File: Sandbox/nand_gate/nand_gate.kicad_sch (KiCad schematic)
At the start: 10 parts, among them Q1 2N3904, Q2 2N3904, Q3 2N3904, SW1 SW_SPST, SW2 SW_SPST

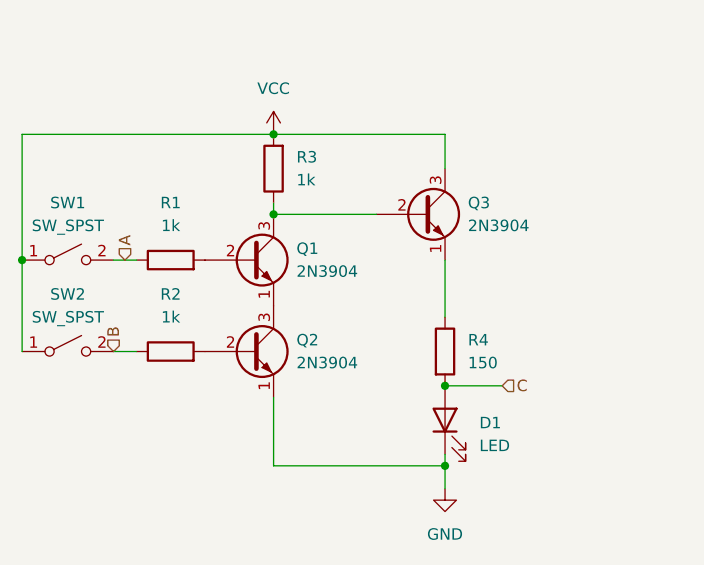
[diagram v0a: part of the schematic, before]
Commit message: Layout for nand gate
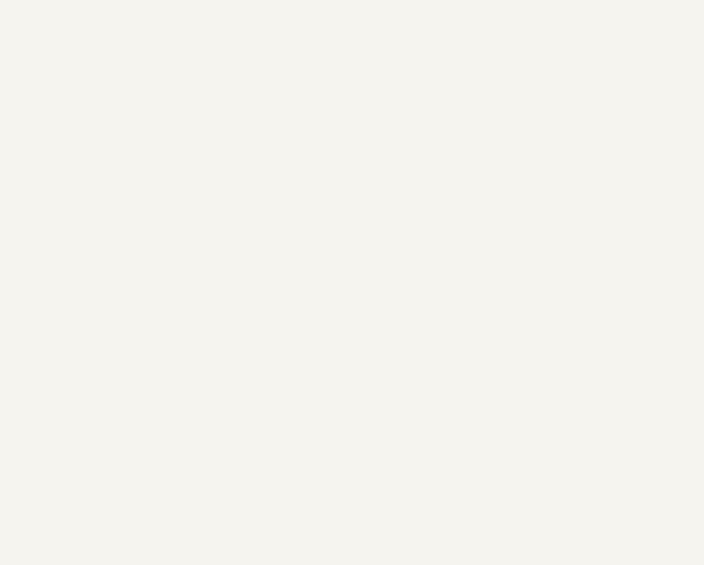
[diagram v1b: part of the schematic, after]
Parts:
- removed D1: LED, LED_THT:LED_D5.0mm, symbol Device:LED
- removed Q1, Q2, Q3: 2N3904, Package_TO_SOT_THT:TO-92_Inline, symbol Transistor_BJT:2N3904
- removed R1, R2, R3: 1k, Resistor_THT:R_Axial_DIN0207_L6.3mm_D2.5mm_P7.62mm_Horizontal, symbol Device:R
- removed R4: 150, Resistor_THT:R_Axial_DIN0207_L6.3mm_D2.5mm_P7.62mm_Horizontal, symbol Device:R
- removed SW1, SW2: SW_SPST, Button_Switch_THT:SW_PUSH_6mm, symbol Switch:SW_SPST

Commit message: Moved Some Things Around
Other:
- added sheet nand_gate7 (nand__gate.kicad_sch)
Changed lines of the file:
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@@
+    )
+  )
+  (sheet (at 83.82 114.3) (size 12.7 8.89) (fields_autoplaced)
+    (stroke (width 0.1524) (type solid))
+    (fill (color 0 0 0 0.0000))
+    (property "Sheetname" "nand_gate7" (at 83.82 113.5884 0)
+      (effects (font (size 1.27 1.27)) (justify left bottom))
+    )
+    (property "Sheetfile" "nand__gate.kicad_sch" (at 83.82 123.7746 0)
+      (effects (font (size 1.27 1.27)) (justify left top))
+    )
+    (pin "B" input (at 83.82 121.92 180)
+      (effects (font (size 1.27 1.27)) (justify left))
+    )
+    (pin "A" input (at 83.82 115.57 180)
+      (effects (font (size 1.27 1.27)) (justify left))
+    )
+    (pin "C" input (at 96.52 118.11 0)
+      (effects (font (size 1.27 1.27)) (justify right))
+    )
+    (instances
+      (project "nand_gate"
+        (path "/ae45e9d9-ebb5-4d6c-8dad-99eadd2be5c5/2e87dc14-878c-467c-8594-4a57b58f886f/6b230bbb-3b41-4fd2-a79b-e0cf50894ec7/0ad4044b-a9cd-452a-a5d6-d186c7bbd4c9" (page "5"))
+        (path "/ae45e9d9-ebb5-4d6c-8dad-99eadd2be5c5/2e87dc14-878c-467c-8594-4a57b58f886f/ec238f57-a4a9-49ac-b4d6-5b2cf534f59d/0ad4044b-a9cd-452a-a5d6-d186c7bbd4c9" (page "13"))
+        (path "/ae45e9d9-ebb5-4d6c-8dad-99eadd2be5c5/2e87dc14-878c-467c-8594-4a57b58f886f" (page "19"))
+        (path "/ae45e9d9-ebb5-4d6c-8dad-99eadd2be5c5" (page "19"))
+      )
     )
   )

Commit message: woring on layout.
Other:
- added sheet D-Latch2 (D-Latch.kicad_sch)
- added sheet SR-Latch1 (SR_LATCH.kicad_sch)
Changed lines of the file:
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@@
+    )
+  )
+  (sheet (at 96.52 26.67) (size 29.21 20.32) (fields_autoplaced)
+    (stroke (width 0.1524) (type solid))
+    (fill (color 0 0 0 0.0000))
+    (property "Sheetname" "D-Latch2" (at 96.52 25.9584 0)
+      (effects (font (size 1.27 1.27)) (justify left bottom))
+    )
+    (property "Sheetfile" "D-Latch.kicad_sch" (at 96.52 47.5746 0)
+      (effects (font (size 1.27 1.27)) (justify left top))
+    )
+    (pin "Data" input (at 96.52 30.48 180)
+      (effects (font (size 1.27 1.27)) (justify left))
+    )
+    (pin "Enable" input (at 96.52 41.91 180)
+      (effects (font (size 1.27 1.27)) (justify left))
+    )
+    (pin "!Q" input (at 125.73 41.91 0)
+      (effects (font (size 1.27 1.27)) (justify right))
+    )
+    (pin "Q" input (at 125.73 31.75 0)
+      (effects (font (size 1.27 1.27)) (justify right))
+    )
+    (instances
+      (project "nand_gate"
+        (path "/ae45e9d9-ebb5-4d6c-8dad-99eadd2be5c5/2e87dc14-878c-467c-8594-4a57b58f886f" (page "10"))
+        (path "/ae45e9d9-ebb5-4d6c-8dad-99eadd2be5c5" (page "23"))
+      )
     )
   )
@@
       )
     )
+  )
+  (sheet (at 57.15 59.69) (size 17.78 13.97) (fields_autoplaced)
+    (stroke (width 0.1524) (type solid))
+    (fill (color 0 0 0 0.0000))
+    (property "Sheetname" "SR-Latch1" (at 57.15 58.9784 0)
+      (effects (font (size 1.27 1.27)) (justify left bottom))
+    )
+    (property "Sheetfile" "SR_LATCH.kicad_sch" (at 57.15 74.2446 0)
+      (effects (font (size 1.27 1.27)) (justify left top))
+    )
+    (pin "Reset" input (at 57.15 72.39 180)
+      (effects (font (size 1.27 1.27)) (justify left))
+    )
+    (pin "Q" input (at 74.93 60.96 0)
+      (effects (font (size 1.27 1.27)) (justify right))
+    )
+    (pin "Set" input (at 57.15 60.96 180)
+      (effects (font (size 1.27 1.27)) (justify left))
+    )
+    (pin "!Q" input (at 74.93 72.39 0)
+      (effects (font (size 1.27 1.27)) (justify right))
+    )
+    (instances
+      (project "nand_gate"
+        (path "/ae45e9d9-ebb5-4d6c-8dad-99eadd2be5c5/2e87dc14-878c-467c-8594-4a57b58f886f/6b230bbb-3b41-4fd2-a79b-e0cf50894ec7" (page "4"))
+        (path "/ae45e9d9-ebb5-4d6c-8dad-99eadd2be5c5/2e87dc14-878c-467c-8594-4a57b58f886f/ec238f57-a4a9-49ac-b4d6-5b2cf534f59d" (page "15"))
+        (path "/ae45e9d9-ebb5-4d6c-8dad-99eadd2be5c5" (page "22"))
+      )
+    )
